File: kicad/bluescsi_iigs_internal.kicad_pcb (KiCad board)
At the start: 2 copper layers, 61.5 x 55.4 mm, 27 parts, among them J1 Conn_02x13_Odd_Even, J2 Conn_02x13_Odd_Even, J3 105162-0001, J4 Conn_01x02_Male, J5 Conn_01x02_Male, J6 DB25_Male, M1 Screw_Terminal_01x01, M2 Screw_Terminal_01x01, SW1 SW_SPDT, U1 YAAJ_BluePill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

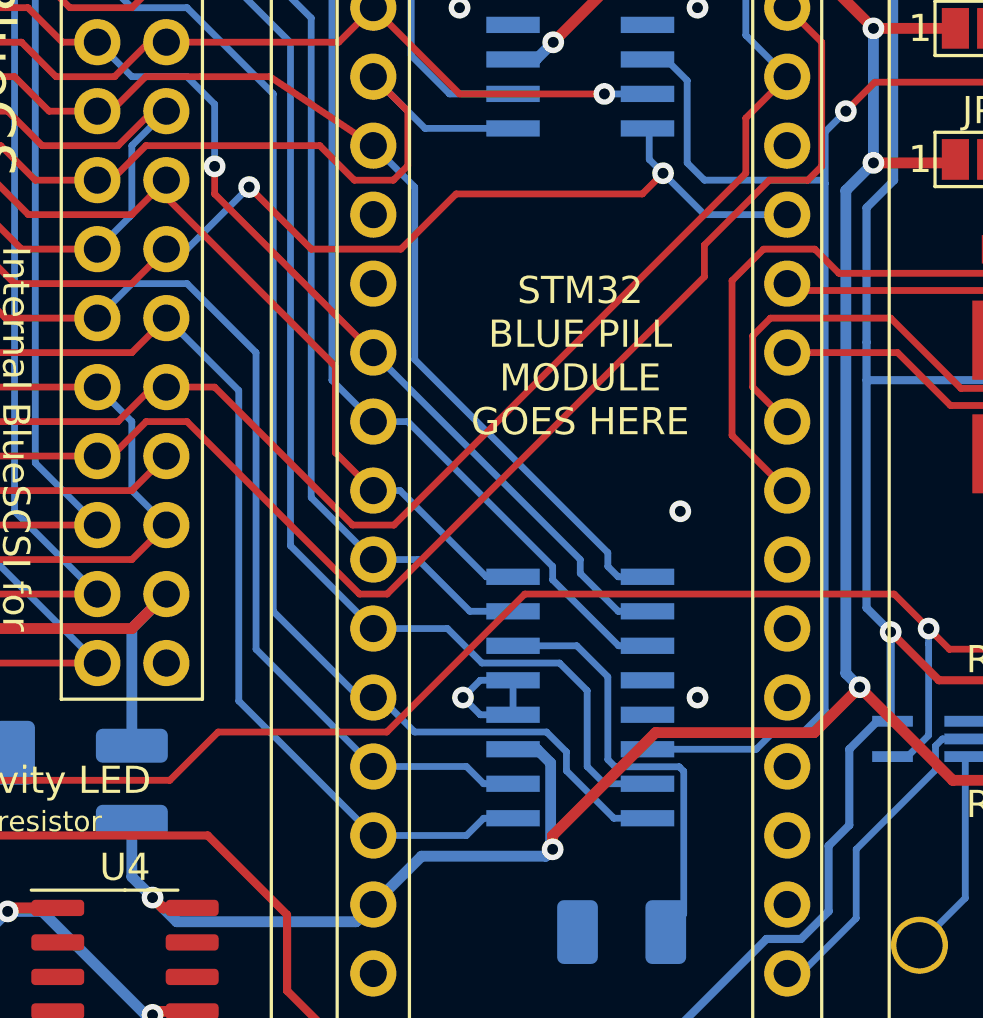
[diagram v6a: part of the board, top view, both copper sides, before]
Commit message: straighter shot for DBP line
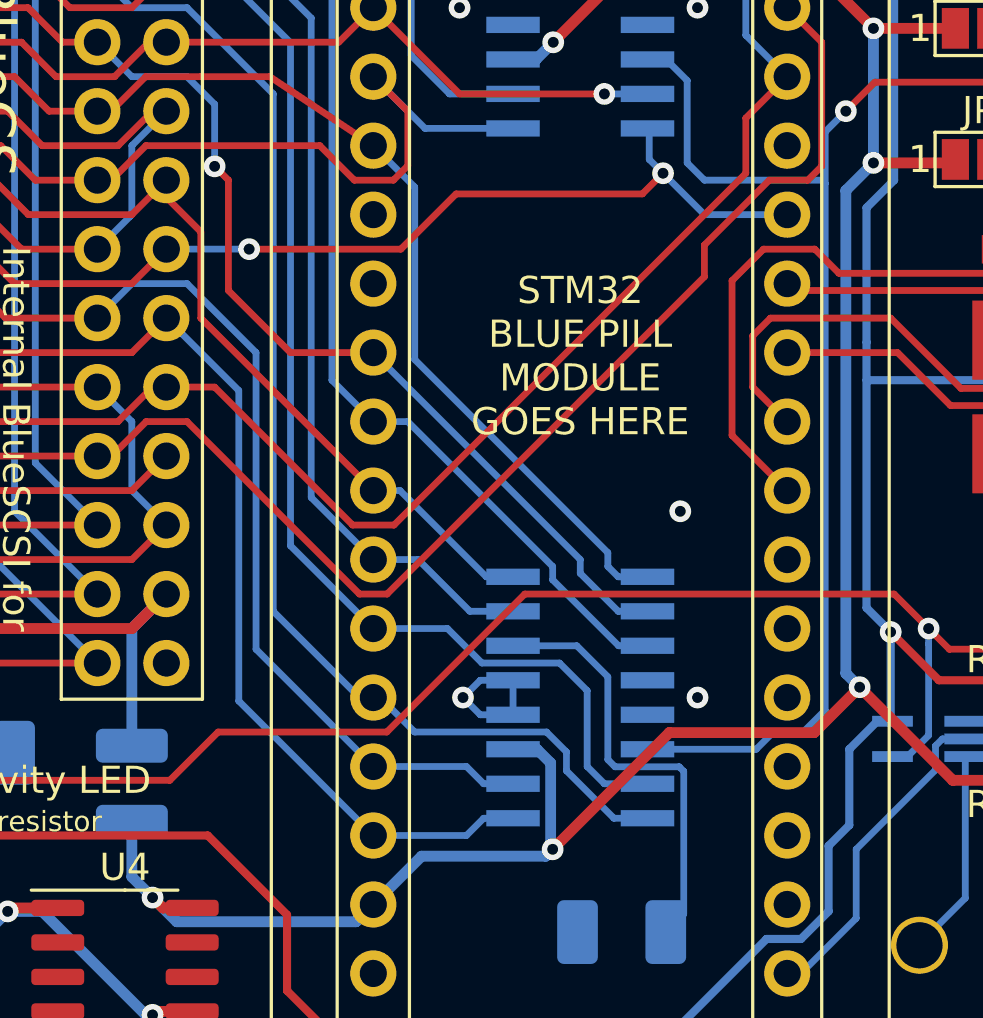
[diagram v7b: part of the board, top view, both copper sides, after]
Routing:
- net /SCSI_DBP: track 48.1 -> 46.2 mm
- net /SCSI_RST: track 49.5 -> 51.2 mm
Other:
- board text added: "WARNING: USB power should not be used while powered from SCSI or Aux Power"
- board text removed: "WARNING: USB power should not be used while powered from SCSI or Aux +12V"
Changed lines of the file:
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@@
     )
     (pad_to_mask_clearance 0)
+    (grid_origin 147.32 67.564)
     (pcbplotparams
       (layerselection 0x0001cfc_ffffffff)
@@
     (effects (font (size 0.75 0.75) (thickness 0.125)) (justify mirror))
   )
-  (gr_text "WARNING: USB\npower should\nnot be used\nwhile powered\nfrom SCSI\nor Aux +12V" (at 160.02 73.66) (layer "B.SilkS")
+  (gr_text "WARNING: USB\npower should\nnot be used\nwhile powered\nfrom SCSI\nor Aux Power" (at 160.02 73.66) (layer "B.SilkS")
     (effects (font (size 1 1) (thickness 0.15)) (justify mirror))
   )
@@
     (style (thickness 0.15) (arrow_length 1.27) (text_position_mode 0) (extension_height 0.58642) (extension_offset 0) keep_text_aligned)
   )
-  (segment (start 162.793511 87.650489) (end 168.635511 87.650489) (width 0.4) (layer "F.Cu") (net 12))
   (segment (start 173.736 89.408) (end 170.307 85.979) (width 0.4) (layer "F.Cu") (net 12))
   (segment (start 159.02532 62.233641) (end 161.58796 59.671001) (width 0.4) (layer "F.Cu") (net 12))
+  (segment (start 163.301511 87.650489) (end 168.635511 87.650489) (width 0.4) (layer "F.Cu") (net 12))
+  (segment (start 159.004 91.948) (end 163.301511 87.650489) (width 0.4) (layer "F.Cu") (net 12))
   (segment (start 144.653 94.107) (end 145.731 94.107) (width 0.4) (layer "F.Cu") (net 12))
   (segment (start 176.927 89.408) (end 173.736 89.408) (width 0.4) (layer "F.Cu") (net 12))
   (segment (start 161.58796 59.671001) (end 168.764001 59.671001) (width 0.4) (layer "F.Cu") (net 12))
-  (segment (start 168.635511 87.650489) (end 170.307 85.979) (width 0.4) (layer "F.Cu") (net 12))
-  (segment (start 159.004 91.44) (end 162.793511 87.650489) (width 0.4) (layer "F.Cu") (net 12))
   (segment (start 168.764001 59.671001) (end 170.815 61.722) (width 0.4) (layer "F.Cu") (net 12))
   (segment (start 144.272 93.726) (end 144.653 94.107) (width 0.4) (layer "F.Cu") (net 12))
+  (segment (start 168.635511 87.650489) (end 170.307 85.979) (width 0.4) (layer "F.Cu") (net 12))
   (segment (start 173.579 66.675) (end 170.814998 66.675) (width 0.4) (layer "F.Cu") (net 12))
   (segment (start 173.833 61.722) (end 170.815 61.722) (width 0.4) (layer "F.Cu") (net 12))
-  (segment (start 159.004 91.948) (end 159.004 91.44) (width 0.4) (layer "F.Cu") (net 12))
   (segment (start 173.833 66.421) (end 173.579 66.675) (width 0.4) (layer "F.Cu") (net 12))
   (via (at 144.272 93.726) (size 0.8) (drill 0.4) (layers "F.Cu" "B.Cu") (net 12))
@@
   (segment (start 137.922 69.85) (end 139.192 71.12) (width 0.25) (layer "F.Cu") (net 17))
   (segment (start 139.192 71.12) (end 143.51 71.12) (width 0.25) (layer "F.Cu") (net 17))
-  (segment (start 155.448 67.818) (end 153.416 69.85) (width 0.25) (layer "F.Cu") (net 17))
-  (segment (start 153.416 69.85) (end 150.114 69.85) (width 0.25) (layer "F.Cu") (net 17))
-  (segment (start 162.306 67.818) (end 155.448 67.818) (width 0.25) (layer "F.Cu") (net 17))
-  (segment (start 150.114 69.85) (end 147.828 67.564) (width 0.25) (layer "F.Cu") (net 17))
-  (segment (start 163.068 67.056) (end 162.306 67.818) (width 0.25) (layer "F.Cu") (net 17))
+  (segment (start 162.306 67.818) (end 163.068 67.056) (width 0.25) (layer "F.Cu") (net 17))
+  (segment (start 147.828 69.85) (end 153.416 69.85) (width 0.25) (layer "F.Cu") (net 17))
+  (segment (start 153.416 69.85) (end 155.448 67.818) (width 0.25) (layer "F.Cu") (net 17))
+  (segment (start 155.448 67.818) (end 162.306 67.818) (width 0.25) (layer "F.Cu") (net 17))
   (via (at 163.068 67.056) (size 0.8) (drill 0.4) (layers "F.Cu" "B.Cu") (net 17))
-  (via (at 147.828 67.564) (size 0.8) (drill 0.4) (layers "F.Cu" "B.Cu") (net 17))
+  (via (at 147.828 69.85) (size 0.8) (drill 0.4) (layers "F.Cu" "B.Cu") (net 17))
   (segment (start 129.038 68.58) (end 133.35 68.58) (width 0.25) (layer "B.Cu") (net 17))
-  (segment (start 147.828 67.564) (end 145.542 69.85) (width 0.25) (layer "B.Cu") (net 17))
   (segment (start 127.883 67.425) (end 129.038 68.58) (width 0.25) (layer "B.Cu") (net 17))
   (segment (start 163.068 67.056) (end 164.592 68.58) (width 0.25) (layer "B.Cu") (net 17))
-  (segment (start 145.542 69.85) (end 144.78 69.85) (width 0.25) (layer "B.Cu") (net 17))
   (segment (start 163.068 67.056) (end 162.56 66.548) (width 0.25) (layer "B.Cu") (net 17))
   (segment (start 127 67.425) (end 127.883 67.425) (width 0.25) (layer "B.Cu") (net 17))
+  (segment (start 147.828 69.85) (end 144.78 69.85) (width 0.25) (layer "B.Cu") (net 17))
   (segment (start 133.35 68.58) (end 134.62 69.85) (width 0.25) (layer "B.Cu") (net 17))
   (segment (start 164.592 68.58) (end 167.64 68.58) (width 0.25) (layer "B.Cu") (net 17))
@@
   (segment (start 139.7 68.58) (end 143.51 68.58) (width 0.25) (layer "F.Cu") (net 18))
   (segment (start 143.51 68.58) (end 144.78 67.31) (width 0.25) (layer "F.Cu") (net 18))
-  (segment (start 151.003 74.168) (end 151.003 77.343) (width 0.25) (layer "F.Cu") (net 18))
   (segment (start 144.78 67.31) (end 144.78 67.945) (width 0.25) (layer "F.Cu") (net 18))
-  (segment (start 151.003 77.343) (end 152.4 78.74) (width 0.25) (layer "F.Cu") (net 18))
-  (segment (start 144.78 67.945) (end 151.003 74.168) (width 0.25) (layer "F.Cu") (net 18))
+  (segment (start 146.05 72.39) (end 152.4 78.74) (width 0.25) (layer "F.Cu") (net 18))
+  (segment (start 144.78 67.945) (end 146.05 69.215) (width 0.25) (layer "F.Cu") (net 18))
+  (segment (start 146.05 69.215) (end 146.05 72.39) (width 0.25) (layer "F.Cu") (net 18))
   (segment (start 153.385 78.74) (end 156.56 81.915) (width 0.25) (layer "B.Cu") (net 18))
   (segment (start 156.56 81.915) (end 157.545 81.915) (width 0.25) (layer "B.Cu") (net 18))
@@
   (segment (start 139.683949 60.96) (end 140.953949 62.23) (width 0.25) (layer "F.Cu") (net 28))
   (segment (start 140.953949 62.23) (end 142.24 62.23) (width 0.25) (layer "F.Cu") (net 28))
+  (segment (start 147.066 67.31) (end 147.066 71.374) (width 0.25) (layer "F.Cu") (net 28))
   (segment (start 132.08 61.993334) (end 132.08 62.23) (width 0.25) (layer "F.Cu") (net 28))
   (segment (start 127.816666 57.73) (end 132.08 61.993334) (width 0.25) (layer "F.Cu") (net 28))
   (segment (start 127 57.73) (end 127.816666 57.73) (width 0.25) (layer "F.Cu") (net 28))
-  (segment (start 146.558 67.818) (end 152.4 73.66) (width 0.25) (layer "F.Cu") (net 28))
-  (segment (start 146.558 66.802) (end 146.558 67.818) (width 0.25) (layer "F.Cu") (net 28))
+  (segment (start 149.352 73.66) (end 152.4 73.66) (width 0.25) (layer "F.Cu") (net 28))
+  (segment (start 147.066 71.374) (end 149.352 73.66) (width 0.25) (layer "F.Cu") (net 28))
+  (segment (start 146.558 66.802) (end 147.066 67.31) (width 0.25) (layer "F.Cu") (net 28))
   (via (at 146.558 66.802) (size 0.8) (drill 0.4) (layers "F.Cu" "B.Cu") (net 28))
   (segment (start 146.558 64.516) (end 145.542 63.5) (width 0.25) (layer "B.Cu") (net 28))
